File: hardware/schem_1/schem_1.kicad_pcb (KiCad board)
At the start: 4 copper layers, 84.9 x 34.3 mm, 83 parts, among them J1 OV7670_Conn_01x24_MountingPin, J2 Micro_SD_Card, J3 FRONT_PCB_CONNECTOR, J4 BG300-04-X-X-A_REVC, J5 UJ2-MBH-1-SMT, J6 BACK_PCB_CONNECTOR, Q1 NDS332P, SW1 BTN_BOOT, SW2 ESP32_RESET, SW4 DOWN, SW5 UP, SW6 OK, U1 ESP32-WROVER-E-JC, U2 XC6210B332MR, U5 XC6206-2.8V, U6 XC6206-1.2V, U7 128x32_OLED_SSD1306, U8 MCP23017_SO

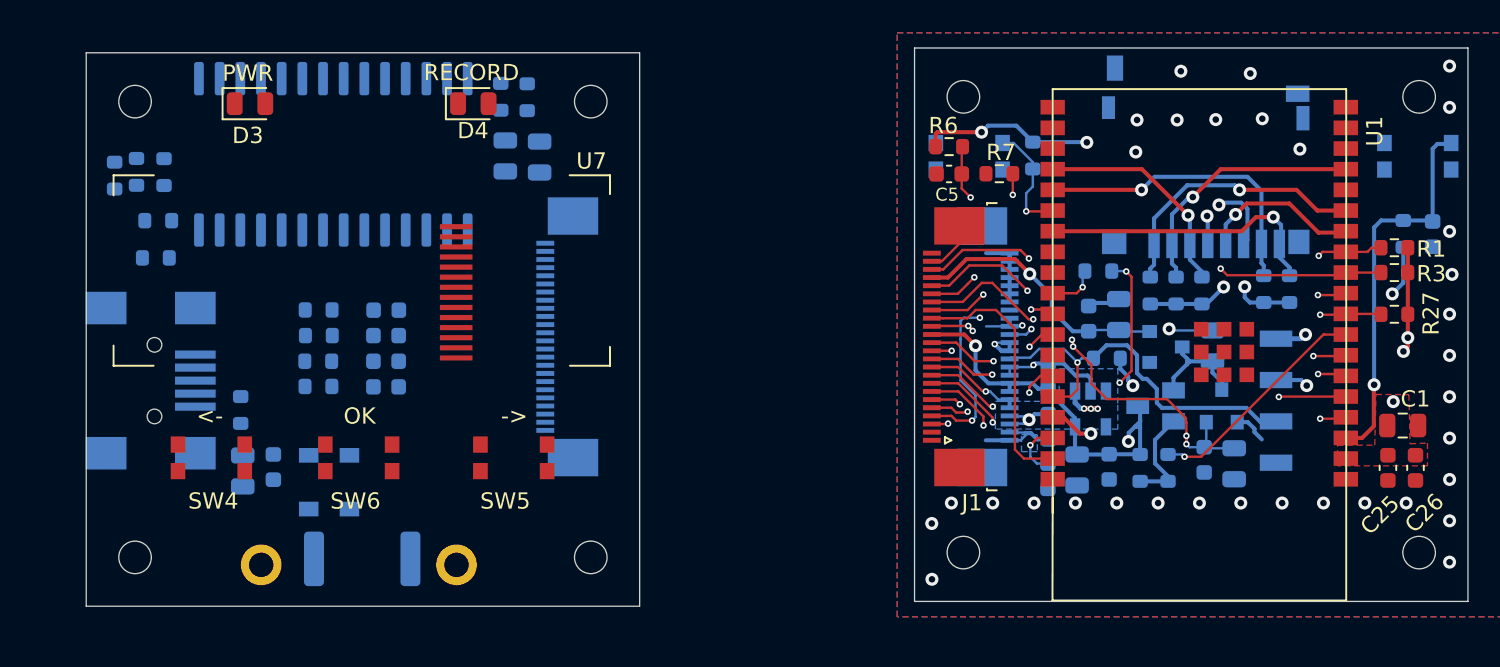
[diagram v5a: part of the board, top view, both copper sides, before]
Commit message: finish laying tracks and the layers on back pcb. modify some footprints as their courtyards were giving errors. 0 drc errors
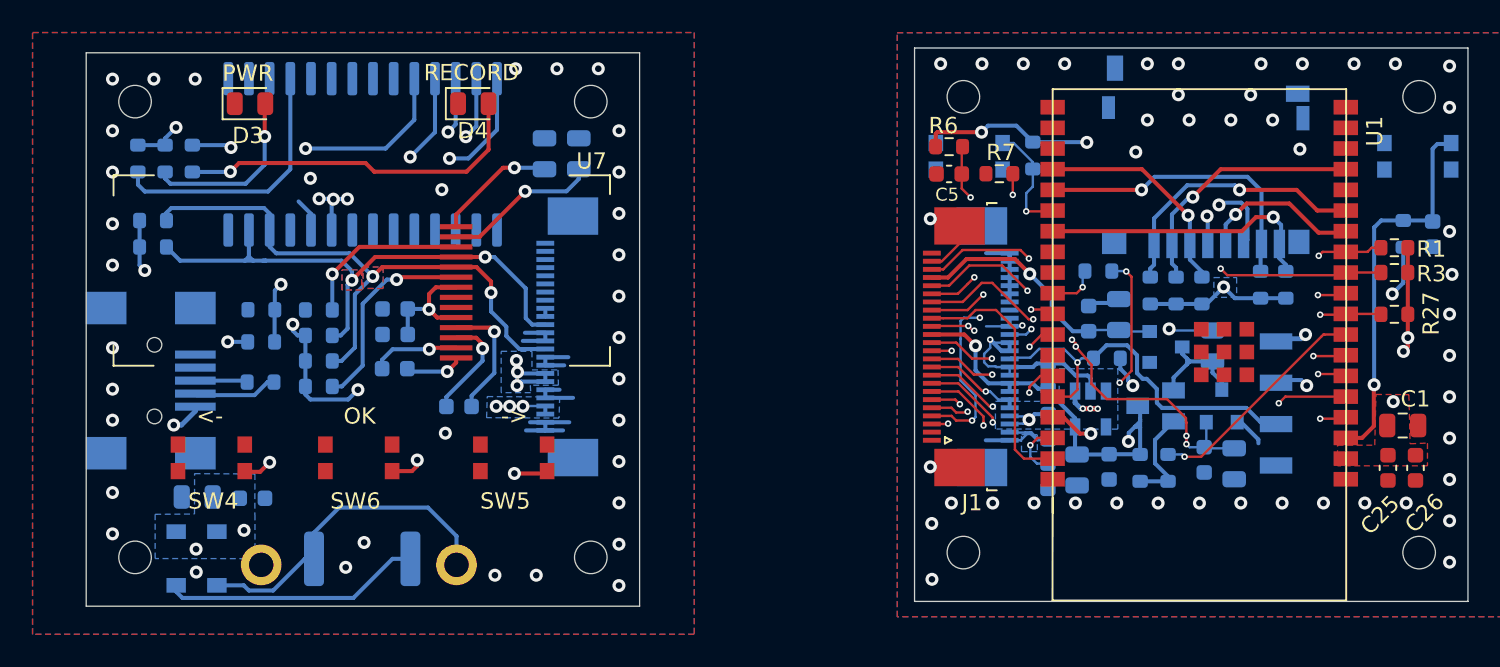
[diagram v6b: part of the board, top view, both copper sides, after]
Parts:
- moved R29 24.2 mm to (62.1, 6.76), turned to 0 degrees
- moved R28 23.3 mm to (62.1, 8.39), turned to 0 degrees
- moved D2 9.40 mm to (63.5, 27.5)
- moved D1 9.40 mm to (66.0, 27.5)
- moved R23 8.37 mm to (68.7, 12.2)
- moved R22 8.27 mm to (68.7, 14.2), turned to 0 degrees
- moved C18 5.28 mm to (80.9, 18.2), turned to 0 degrees
- moved C23 3.22 mm to (64.8, 23.7), turned to 180 degrees
- moved C21 2.42 mm to (88.2, 2.66)
- moved C22 2.41 mm to (86.1, 2.66)
- moved C9 2.31 mm to (68.2, 23.8), turned to 0 degrees
- moved R5 2.10 mm to (68.7, 16.7), turned to 180 degrees
- moved R16 1.94 mm to (62.8, 2.95)
- moved R25 1.93 mm to (64.5, 2.95)
- moved U8 1.80 mm to (74.9, 2.70)
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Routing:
- net /SCL: track 23.9 -> 61.0 mm, vias 1 -> 3
- net /SDA: track 23.5 -> 59.6 mm, vias 2 -> 4
- net +3V3: track 56.9 -> 89.1 mm, vias 12 -> 22
- net /GPIO Expander/BTN_DOWN: track 0.00 -> 30.1 mm, vias 0 -> 2
- net /GPIO Expander/BTN_OK: track 0.00 -> 28.4 mm, vias 0 -> 2
- net /GPIO Expander/BTN_UP: track 0.00 -> 27.8 mm, vias 0 -> 2
- net Net-(D4-Pad2): track 0.00 -> 22.0 mm, vias 0 -> 1
- net GND: track 45.2 -> 65.9 mm, vias 39 -> 85
- net Net-(C2-Pad1): track 0.00 -> 20.4 mm
- net /GPIO Expander/Vusb_detect: track 0.00 -> 20.3 mm, vias 0 -> 2
- net /GPIO Expander/LED_RECORDING: track 0.00 -> 17.0 mm, vias 0 -> 2
- net Net-(R24-Pad2): track 0.00 -> 16.4 mm
- net Net-(D2-Pad1): track 0.00 -> 15.9 mm
- net /I2C OLED/OLED_RESET: track 0.00 -> 12.6 mm, vias 0 -> 1
- net Net-(D3-Pad2): track 0.00 -> 10.9 mm, vias 0 -> 1
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- added copper zone on B.Cu, net +3V3
- added copper zone on B.Cu, net /SCL
- added copper zone on F.Cu, net /SCL
- added copper zone on B.Cu, net /SDA
- added copper zone on F.Cu, net /SDA
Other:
- board text added: "F.CU : Signal In1.Cu : Power In2.Cu: Signal B.Cu : Signal"

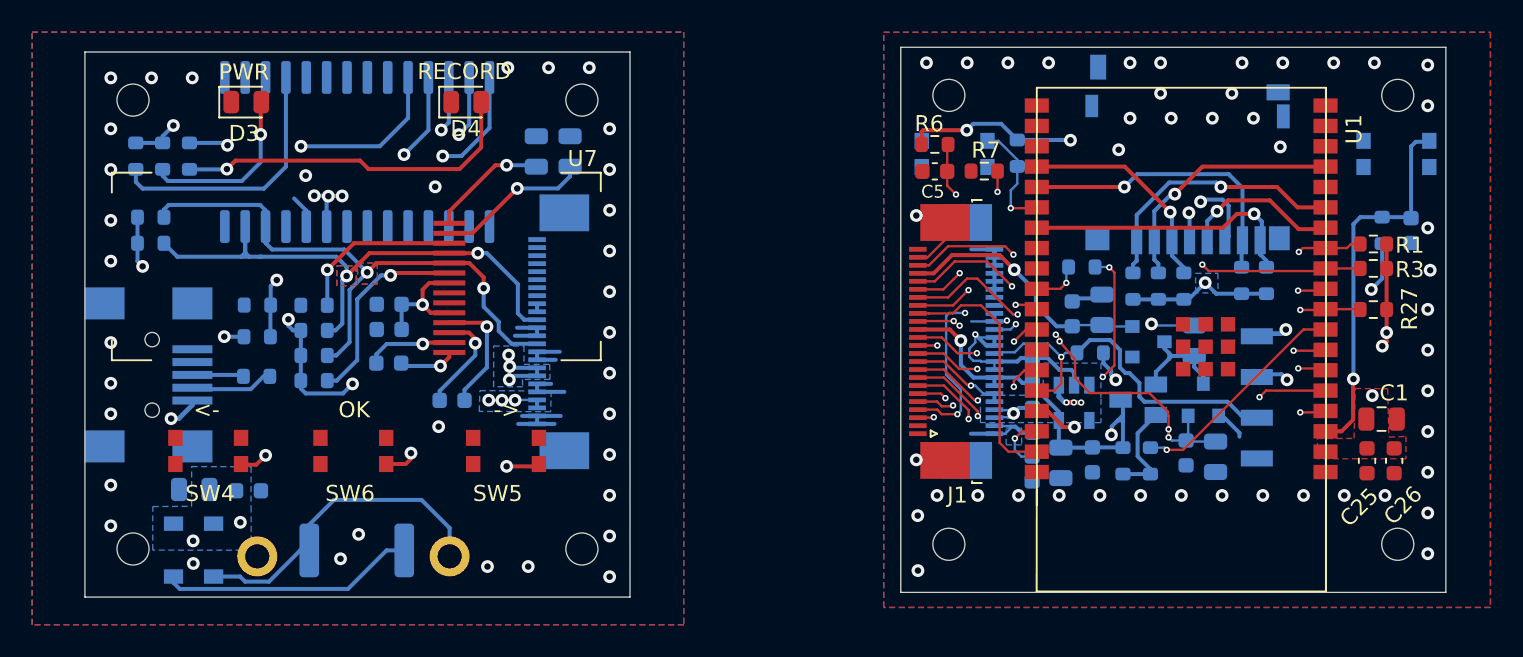
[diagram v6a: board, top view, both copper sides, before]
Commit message: joined the PCBs together with mouse bites
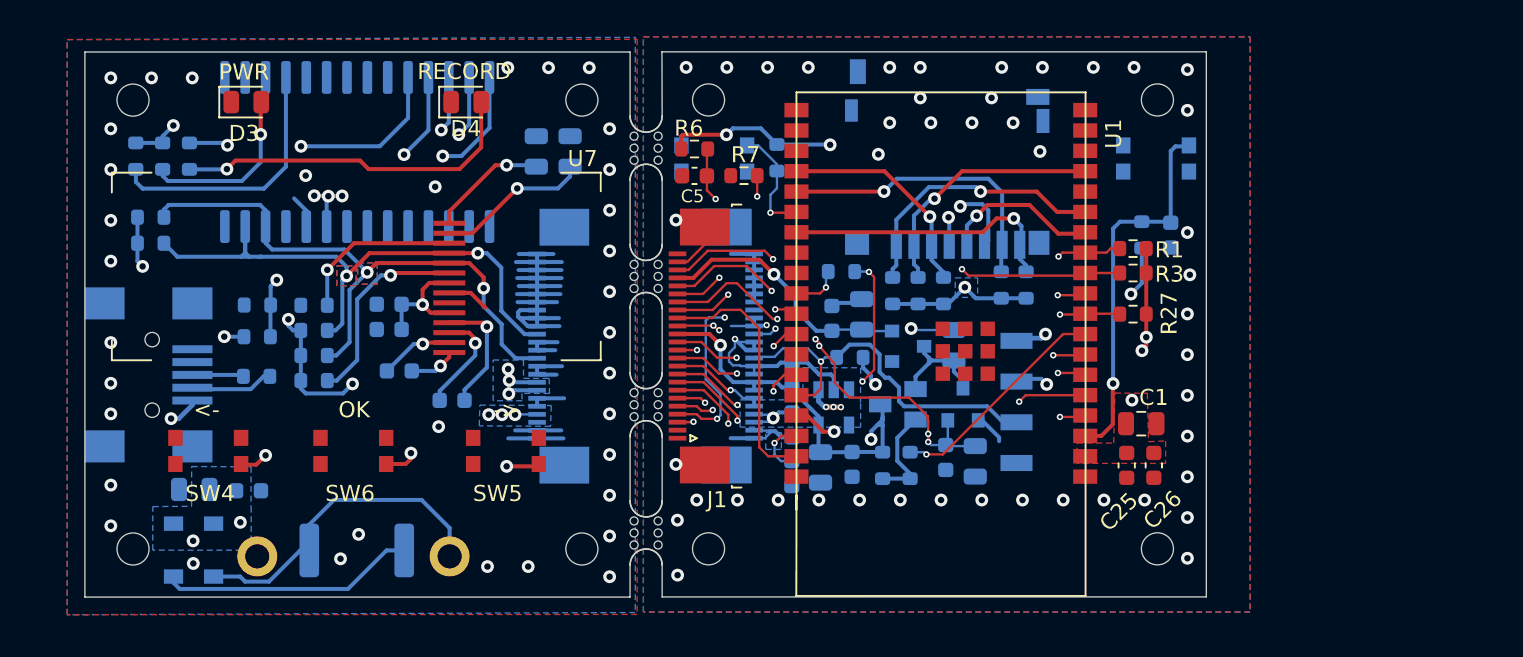
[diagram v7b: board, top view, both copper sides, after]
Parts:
- added mouse-bite-2mm-slot: VAL**, Panelization:mouse-bite-2mm-slot, F.Cu at (93.0, 26.5)
- added mouse-bite-2mm-slot: VAL**, Panelization:mouse-bite-2mm-slot, F.Cu at (93.0, 18.5)
- added mouse-bite-2mm-slot: VAL**, Panelization:mouse-bite-2mm-slot, F.Cu at (93.0, 2.46)
- added mouse-bite-2mm-slot: VAL**, Panelization:mouse-bite-2mm-slot, F.Cu at (93.0, 10.5)
- moved C26 15.0 mm to (124.6, 22.2)
- moved R15 15.0 mm to (116.7, 11.0)
- moved C10 15.0 mm to (106.4, 12.8)
- moved C11 15.0 mm to (104.6, 13.1)
- moved C12 15.0 mm to (102.1, 19.7)
- moved C14 15.0 mm to (113.5, 22.0)
- moved C15 15.0 mm to (111.7, 21.7)
- moved C16 15.0 mm to (112.2, 14.8)
- moved C24 15.0 mm to (105.8, 22.2)
- moved C25 15.0 mm to (122.9, 22.2)
- moved C3 15.0 mm to (102.1, 22.8)
- moved C4 15.0 mm to (102.1, 16.6)
- moved C5 15.0 mm to (96.0, 4.18)
- moved C8 15.0 mm to (103.8, 22.4)
- moved H1 15.0 mm to (96.9, 27.4)
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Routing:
- net GND: track 65.9 -> 99.0 mm
- net /SDA: track 59.6 -> 60.5 mm
- net Net-(C17-Pad2): track 5.40 -> 4.62 mm
- net /SCL: track 61.0 -> 61.8 mm
- net Net-(C17-Pad1): track 3.59 -> 2.99 mm
- net /5V_USB_SC: track 30.3 -> 29.8 mm
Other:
- board size 84.9 x 34.3 mm -> 69.9 x 34 mm

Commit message: update to latest gerbers, update project plan
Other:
- board text removed: "1 GND"
